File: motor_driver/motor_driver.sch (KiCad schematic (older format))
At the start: 7 parts

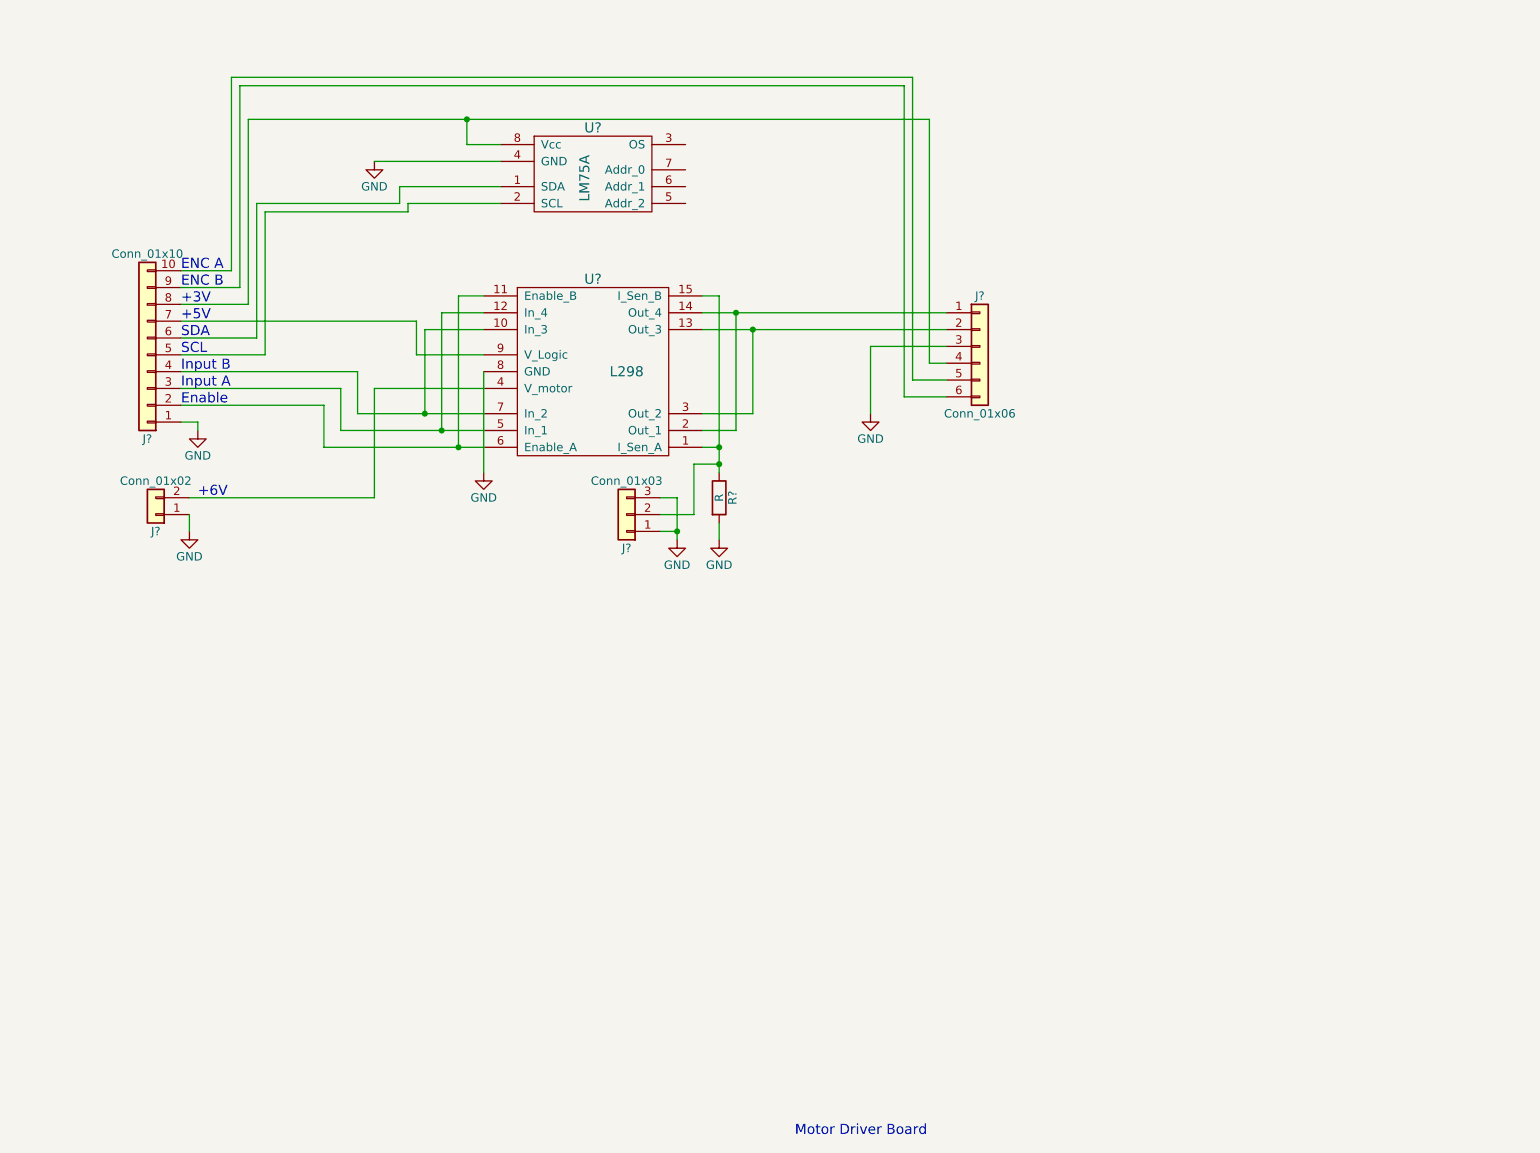
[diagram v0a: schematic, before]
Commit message: added power caps and pull resistors
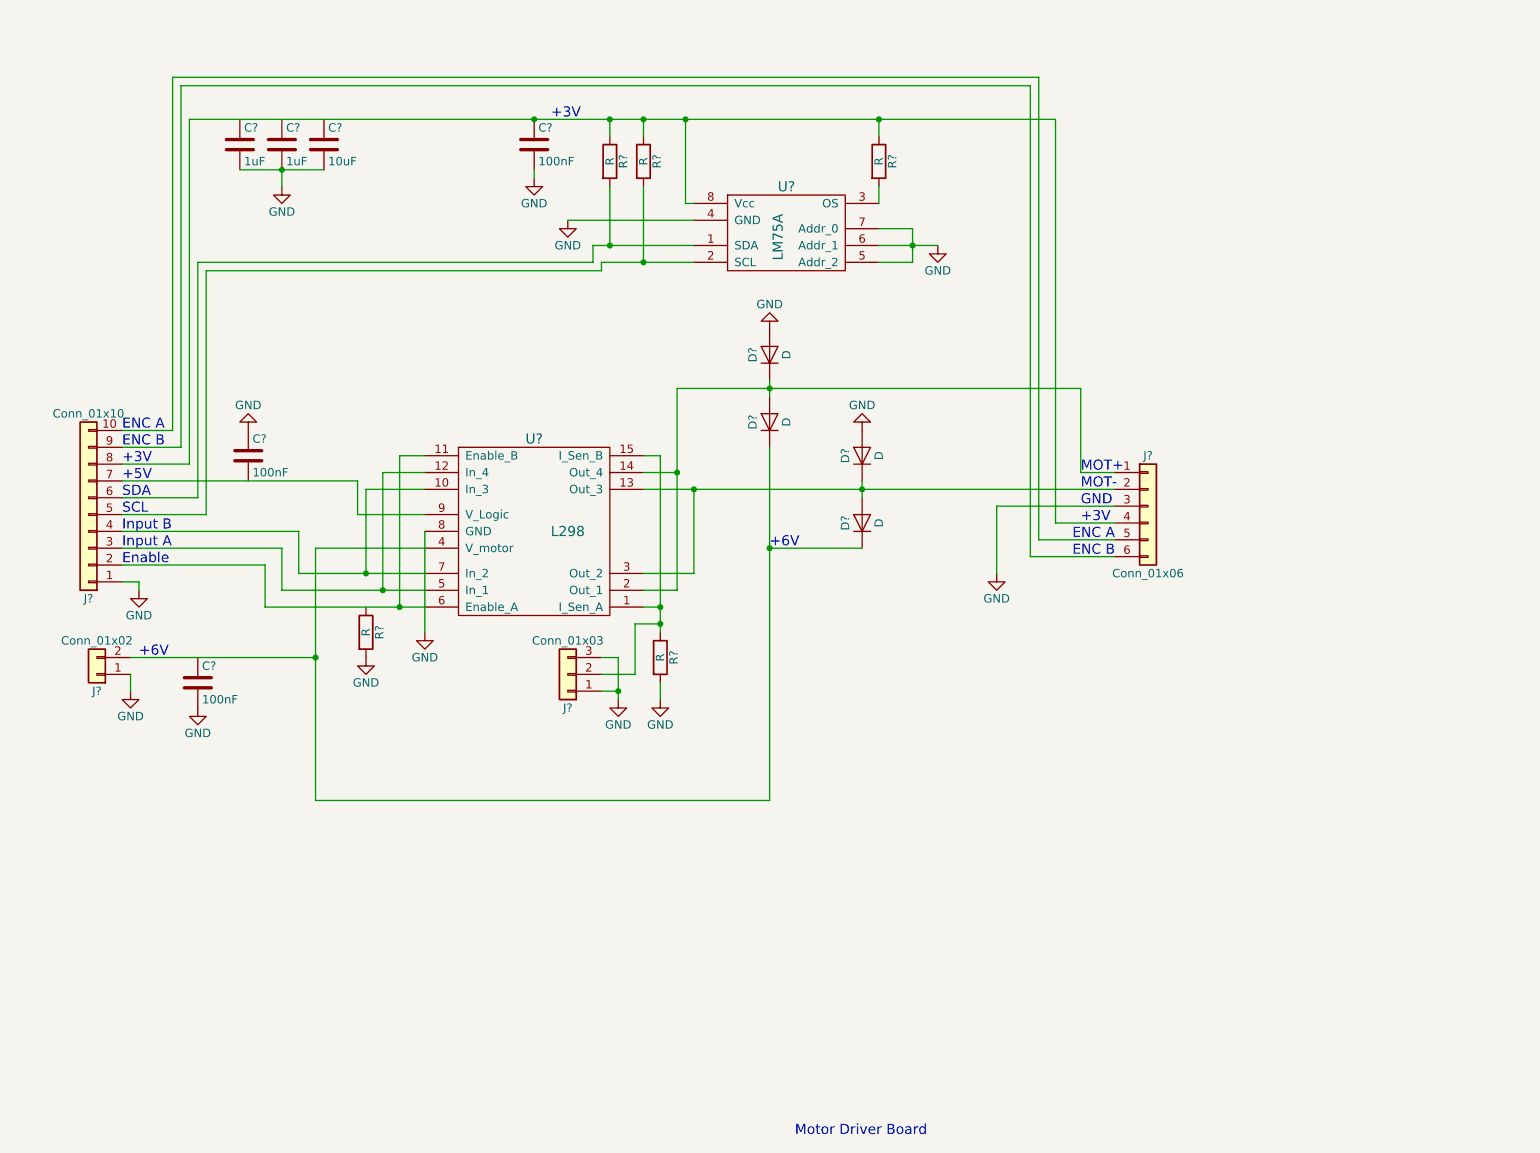
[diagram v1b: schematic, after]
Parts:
- added C? (x3): 100nF, symbol C
- added C? (x2): 1uF, symbol C
- added C?: 10uF, symbol C
- added D? (x4): D, symbol D
- added R? (x4): R, symbol R
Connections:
- net GND: now also U?.5 (Addr_2), U?.6 (Addr_1), U?.7 (Addr_0), C?.1, C?.2, C?.2, C?.2, C?.2, C?.2, D?.2 (A), D?.2 (A), R?.2
- net at J?.2 (Pin_2), U?.13 (Out_3), U?.3 (Out_2): now also D?.1 (K), D?.2 (A)
- net at J?.1 (Pin_1), U?.14 (Out_4), U?.2 (Out_1): now also D?.1 (K), D?.2 (A)
- net at J?.2 (Pin_2), U?.4 (V_motor): now also D?.1 (K), D?.1 (K)
- net at J?.6 (Pin_6), U?.1 (SDA): now also R?.2
- net at J?.5 (Pin_5), U?.2 (SCL): now also R?.2
- net at U?.3 (OS): now also R?.2
- net at J?.4 (Pin_4), J?.8 (Pin_8), U?.8 (Vcc): now also C?.1, R?.1, R?.1, R?.1
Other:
- note added: "GND"
- note added: "MOT+"
- note added: "MOT-"
- moved on the sheet: J?, R?, U?

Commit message: basic board layout done
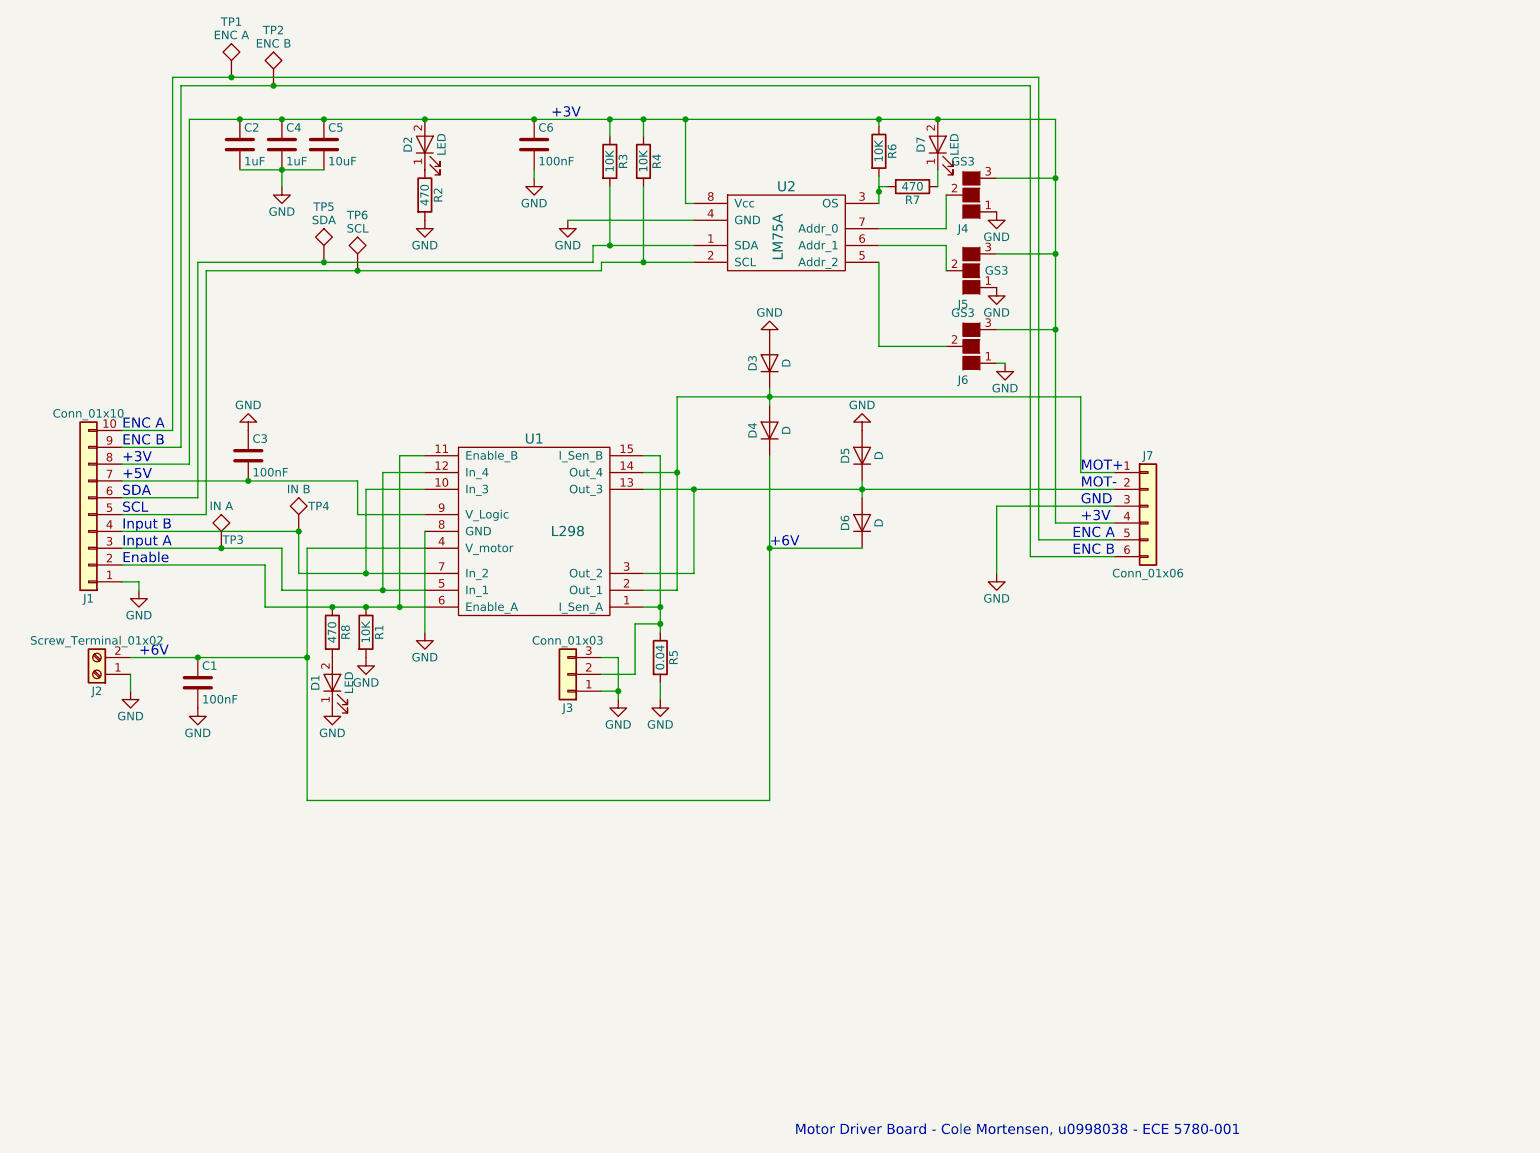
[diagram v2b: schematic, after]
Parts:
- removed J?: Conn_01x02, symbol Conn_01x02
- added D1, D2, D7: LED, LEDs:LED_1206_HandSoldering, symbol LED
- added J2: Screw_Terminal_01x02, TerminalBlocks_Phoenix:TerminalBlock_Phoenix_MKDS1.5-2pol, symbol Screw_Terminal_01x02
- added J4, J5, J6: GS3, Connectors:GS3, symbol GS3
- added R2, R7, R8: 470, Resistors_SMD:R_1206_HandSoldering, symbol R
- added TP1: ENC A, Measurement_Points:Test_Point, symbol TEST
- added TP2: ENC B, Measurement_Points:Test_Point, symbol TEST
- added TP3: IN A, Measurement_Points:Measurement_Point_Round-SMD-Pad_Small, symbol TEST
- added TP4: IN B, Measurement_Points:Measurement_Point_Round-SMD-Pad_Small, symbol TEST
- added TP5: SDA, Measurement_Points:Test_Point, symbol TEST
- added TP6: SCL, Measurement_Points:Test_Point, symbol TEST
- C1, C3, C6: renamed from C?; footprint (none) -> Capacitors_SMD:C_1206_HandSoldering
- C2, C4: renamed from C?; footprint (none) -> Capacitors_THT:CP_Radial_D5.0mm_P2.00mm
- C5: renamed from C?; footprint (none) -> Capacitors_THT:C_Rect_L7.0mm_W3.5mm_P5.00mm
- D3, D4, D5, D6: renamed from D?; footprint (none) -> Diodes_SMD:D_SMA_Handsoldering
- J1: renamed from J?; footprint (none) -> Socket_Strips:Socket_Strip_Straight_1x10_Pitch2.54mm
- J3: renamed from J?; footprint (none) -> Socket_Strips:Socket_Strip_Straight_1x03_Pitch2.54mm
- J7: renamed from J?; footprint (none) -> Socket_Strips:Socket_Strip_Straight_1x06_Pitch2.54mm
- R1, R3, R4, R6: renamed from R?; value R -> 10K; footprint (none) -> Resistors_SMD:R_1206_HandSoldering
- R5: renamed from R?; value R -> 0.04; footprint (none) -> Resistors_SMD:R_1206_HandSoldering
- U1: renamed from U?; footprint (none) -> TO_SOT_Packages_THT:TO-220-15_Vertical_StaggeredType1
- U2: renamed from U?; footprint (none) -> SMD_Packages:SOIC-8-N
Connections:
- net GND: now also D1.1 (K), J2.1 (Pin_1), J4.1 (G1), J5.1 (G1), J6.1 (G1), R2.2; no longer U2.5 (Addr_2), U2.6 (Addr_1), U2.7 (Addr_0)
- net at J1.4 (Pin_4), U1.10 (In_3), U1.7 (In_2): now also TP4.1
- net at J1.2 (Pin_2), U1.11 (Enable_B), U1.6 (Enable_A): now also R1.1, R8.1
- net at J1.3 (Pin_3), U1.12 (In_4), U1.5 (In_1): now also TP3.1
- net at D4.1 (K), D6.1 (K), U1.4 (V_motor): now also C1.1, J2.2 (Pin_2)
- net at J1.7 (Pin_7), U1.9 (V_Logic): now also C3.2
- net at J1.6 (Pin_6), R3.2, U2.1 (SDA): now also TP5.1
- net at J1.5 (Pin_5), R4.2, U2.2 (SCL): now also TP6.1
- net at R6.2, U2.3 (OS): now also R7.2
- net at C6.1, J1.8 (Pin_8), J7.4 (Pin_4)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: now also C2.1, C4.1, C5.1, D2.2 (A), D7.2 (A), J4.3 (G3), J5.3 (G3), J6.3 (G3)
- net at J1.10 (Pin_10), J7.5 (Pin_5): now also TP1.1
- net at J1.9 (Pin_9), J7.6 (Pin_6): now also TP2.1
- new net: J6.2 (G2), U2.5 (Addr_2)
- new net: J5.2 (G2), U2.6 (Addr_1)
- new net: J4.2 (G2), U2.7 (Addr_0)
- new net: D7.1 (K), R7.1
- new net: D2.1 (K), R2.1
- new net: D1.2 (A), R8.2
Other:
- note added: "Motor Driver Board - Cole Mortensen, u0998038 - ECE 5780-001\n"
- note removed: "Motor Driver Board\n"
- moved on the sheet: D3, D4, R6

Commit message: routing finished, need to do silkscreen
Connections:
- net at C3.2, J1.7 (Pin_7), U1.9 (V_Logic): now also J7.4 (Pin_4)
- net at C2.1, C4.1, C5.1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: no longer J7.4 (Pin_4)
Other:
- note added: "The sense resistor was sized at 0.04 ohms. This would allow for a max voltage of \n0.1 volts. This will give us enough resolution on the ADC for effective current\nsensing. A 10uF and two 1uF capacitors are used on the 3.3V line for voltage\nsmoothing and for the various LEDs powered by the rail."
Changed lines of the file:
@@
 +3V
 Text Notes 8350 4100 0    60   ~ 0
-+3V
++5V
 Text Notes 8350 4000 0    60   ~ 0
 GND
@@
 	7850 4000 8550 4000
 Wire Wire Line
-	8200 4100 8550 4100
-Wire Wire Line
-	8200 1700 8200 4100
-Wire Wire Line
 	3050 1700 8200 1700
 Wire Wire Line
@@
 	2650 3850 4050 3850
 Wire Wire Line
-	4050 3850 4050 4050
+	4050 2740 4050 4050
 Wire Wire Line
 	4050 4050 4450 4050
@@
 	7150 2040 7150 2130
 Connection ~ 7150 2130
+Text Notes 6400 7220 0    60   ~ 0
+The sense resistor was sized at 0.04 ohms. This would allow for a max voltage of \n0.1 volts. This will give us enough resolution on the ADC for effective current\nsensing. A 10uF and two 1uF capacitors are used on the 3.3V line for voltage\nsmoothing and for the various LEDs powered by the rail.
+Wire Wire Line
+	8200 2950 8200 1700
+Wire Wire Line
+	4050 2740 6990 2740
+Wire Wire Line
+	6990 2740 6990 3240
+Wire Wire Line
+	6990 3240 7450 3240
+Wire Wire Line
+	7450 3240 7450 4100
+Wire Wire Line
+	7450 4100 8550 4100
+Connection ~ 4050 3850
 $EndSCHEMATC
